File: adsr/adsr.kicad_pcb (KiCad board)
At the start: 2 copper layers, 44 parts, among them J1 B_GATE, J2 A_GATE, J3 B_IN, J4 A_IN, J5 B_OUT, J6 A_OUT, J7 EURORACK_CONN_16, J8 Conn_01x04_Male, Q1 2N3904, Q2 2N3904, Q3 2N3904, Q4 2N3904, U1 LM13700, U2 TL074, U3 DG403, U4 DG403, U5 DG403, U6 DG403

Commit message: rework ASDR
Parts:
- removed C3: 22u, Resistor_THT:R_Axial_DIN0204_L3.6mm_D1.6mm_P2.54mm_Vertical
- removed C4: 100n, Capacitor_THT:C_Rect_L10.0mm_W2.5mm_P7.50mm_MKS4
- removed D2: D, Diode_THT:D_A-405_P7.62mm_Horizontal
- removed Q3, Q4: 2N3904, Package_TO_SOT_THT:TO-92_Inline
- removed R10, R11, R9: 100K, Resistor_THT:R_Axial_DIN0204_L3.6mm_D1.6mm_P2.54mm_Vertical
- removed R12, R8: 1K, Resistor_THT:R_Axial_DIN0204_L3.6mm_D1.6mm_P2.54mm_Vertical
- removed R7: 12K, Resistor_THT:R_Axial_DIN0204_L3.6mm_D1.6mm_P2.54mm_Vertical
- removed RV5: R_SUSTAIN, Connector_PinHeader_2.54mm:PinHeader_1x03_P2.54mm_Vertical
- removed RV6: R_DECAY, Connector_PinHeader_2.54mm:PinHeader_1x03_P2.54mm_Vertical
- removed RV7: R_ATTACK, Connector_PinHeader_2.54mm:PinHeader_1x03_P2.54mm_Vertical
- removed RV8: R_RELEASE, Connector_PinHeader_2.54mm:PinHeader_1x03_P2.54mm_Vertical
- removed U5, U6: DG403, Package_SO:SOIC-16_3.9x9.9mm_P1.27mm
- added C10: 0.1u, Capacitor_SMD:C_1206_3216Metric_Pad1.42x1.75mm_HandSolder, F.Cu at (95.0, 142.2)
- added C7: 0.1u, Capacitor_SMD:C_1206_3216Metric_Pad1.42x1.75mm_HandSolder, F.Cu at (104.8, 158.1)
- added C8: 0.1u, Capacitor_SMD:C_1206_3216Metric_Pad1.42x1.75mm_HandSolder, F.Cu at (104.8, 161.3)
- added C9: 0.1u, Capacitor_SMD:C_1206_3216Metric_Pad1.42x1.75mm_HandSolder, F.Cu at (95.0, 145.4)
- added D3: D, Diode_THT:D_A-405_P2.54mm_Vertical_AnodeUp, F.Cu at (3.56, 71.2)
- added D4: D, Diode_THT:D_A-405_P2.54mm_Vertical_AnodeUp, F.Cu at (3.30, 85.2)
- added J10: Conn_01x08_Male, Connector_PinSocket_2.54mm:PinSocket_1x08_P2.54mm_Vertical, F.Cu at (-18.4, 112.4)
- added J11: Conn_01x08_Female, Connector_PinSocket_2.54mm:PinSocket_1x08_P2.54mm_Vertical, F.Cu at (71.8, 157.2)
- added J12: Conn_01x08_Male, Connector_PinSocket_2.54mm:PinSocket_1x08_P2.54mm_Vertical, F.Cu at (-15.9, 112.4)
- added J9: Conn_01x08_Female, Connector_PinSocket_2.54mm:PinSocket_1x08_P2.54mm_Vertical, F.Cu at (69.2, 157.2)
- added Q5: DMMT5401, Package_TO_SOT_SMD:SOT-23-6_Handsoldering, F.Cu at (109.9, 176.5)
- added R13: 1M, Resistor_SMD:R_1206_3216Metric_Pad1.42x1.75mm_HandSolder, F.Cu at (3.56, 76.3)
- added R14: 1M, Resistor_SMD:R_1206_3216Metric_Pad1.42x1.75mm_HandSolder, F.Cu at (3.30, 90.3)
- added R15: 10K, Resistor_SMD:R_1206_3216Metric_Pad1.42x1.75mm_HandSolder, F.Cu at (79.0, 160.0)
- added R16: 10K, Resistor_SMD:R_1206_3216Metric_Pad1.42x1.75mm_HandSolder, F.Cu at (79.0, 155.6)
- added R19: 6.8k, Resistor_SMD:R_1206_3216Metric_Pad1.42x1.75mm_HandSolder, F.Cu at (111.8, 170.2)
- C1: value 22u -> 4.7u; footprint Resistor_THT:R_Axial_DIN0204_L3.6mm_D1.6mm_P2.54mm_Vertical -> Capacitor_SMD:C_1206_3216Metric_Pad1.42x1.75mm_HandSolder
- C2: footprint Capacitor_THT:C_Rect_L10.0mm_W2.5mm_P7.50mm_MKS4 -> Capacitor_SMD:C_1206_3216Metric_Pad1.42x1.75mm_HandSolder
- D1: footprint Diode_THT:D_A-405_P7.62mm_Horizontal -> Diode_THT:D_A-405_P2.54mm_Vertical_AnodeUp
- J1, J2, J3, J4, J5, J6: footprint synth:3.5MM_Jack_Breakout_Vertical -> synth:Jack_3.5mm_QingPu_WQP-PJ398SM_Vertical_CircularHoles
- R1: value 12K -> 6.8k; footprint Resistor_THT:R_Axial_DIN0204_L3.6mm_D1.6mm_P2.54mm_Vertical -> Resistor_SMD:R_1206_3216Metric_Pad1.42x1.75mm_HandSolder
- R2, R3, R4, R5, R6: footprint Resistor_THT:R_Axial_DIN0204_L3.6mm_D1.6mm_P2.54mm_Vertical -> Resistor_SMD:R_1206_3216Metric_Pad1.42x1.75mm_HandSolder
- RV1: value R_SUSTAIN -> R_ATTACK; footprint Connector_PinHeader_2.54mm:PinHeader_1x03_P2.54mm_Vertical -> synth:Potentiometer_Alpha_RD902F-40-00D_Dual_Vertical
- RV2, RV4: footprint Connector_PinHeader_2.54mm:PinHeader_1x03_P2.54mm_Vertical -> synth:Potentiometer_Alpha_RD902F-40-00D_Dual_Vertical
- RV3: value R_ATTACK -> R_SUSTAIN; footprint Connector_PinHeader_2.54mm:PinHeader_1x03_P2.54mm_Vertical -> synth:Potentiometer_Alpha_RD902F-40-00D_Dual_Vertical
- moved RV3 201.7 mm to (-5.12, 100.3), turned to 270 degrees
- moved RV1 200.9 mm to (-5.12, 59.7), turned to 270 degrees
- moved RV2 200.2 mm to (-5.12, 80.0), turned to 270 degrees
- moved RV4 196.6 mm to (-5.12, 120.7), turned to 270 degrees
- moved R3 178.3 mm to (79.0, 169.5)
- moved Q2 158.5 mm to (125.7, 156.2), turned to 270 degrees
- moved R2 153.8 mm to (78.7, 165.7), turned to 180 degrees
- moved J8 146.6 mm to (1.91, 54.0)
- moved R1 143.1 mm to (107.3, 170.0), turned to 90 degrees
- moved C1 138.6 mm to (107.5, 151.8)
- moved C2 132.6 mm to (119.8, 156.2)
- moved R6 128.8 mm to (125.3, 163.6), turned to 270 degrees
- moved J7 128.0 mm to (99.1, 128.3)
- moved R4 128.0 mm to (133.3, 163.4), turned to 90 degrees
- moved Q1 125.1 mm to (132.7, 156.2), turned to 270 degrees
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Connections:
- J8 pad 1: B_OUT_DEFAULT -> A_IN_DEFAULT
- J8 pad 4: A_IN_DEFAULT -> B_OUT_DEFAULT
- R1 pad 1: Net-(R1-Pad1) -> Net-(Q5-Pad4)
- R2 pad 1: A_IN -> /envelope/REF
- RV1 pad 1: A_IN -> /sheet5F5D80AF/ATTACK
- RV1 pad 2: Net-(RV1-Pad2) -> GND
- RV2 pad 1: +12V -> /sheet5F5D80AF/DECAY
- RV2 pad 2: +12V -> GND
- RV2 pad 3: Net-(RV2-Pad3) -> GND
- RV3 pad 1: +12V -> GND
- RV3 pad 2: +12V -> /sheet5F5D80AF/SUS_RAW
- RV3 pad 3: Net-(RV3-Pad3) -> /sheet5F5D80AF/REF_RAW
- RV4 pad 1: +12V -> /sheet5F5D80AF/RELEASE
- RV4 pad 2: +12V -> GND
- RV4 pad 3: Net-(RV4-Pad3) -> GND
- U2 pad 10: Net-(R8-Pad2) -> /envelope/REF_RAW
- U2 pad 12: Net-(C3-Pad1) -> /envelope/SUS_RAW
- U2 pad 13: B_OUT -> /envelope/SUS
- U2 pad 14: B_OUT -> /envelope/SUS
- U2 pad 6: A_OUT -> Net-(R15-Pad2)
- U2 pad 8: Net-(U1-Pad7) -> /envelope/REF
- U2 pad 9: Net-(C3-Pad1) -> /envelope/REF
- U3 pad 6: Net-(RV1-Pad2) -> /envelope/SUS
- U3 pad 8: A_IN -> /envelope/REF
- U4 pad 1: Net-(RV4-Pad3) -> /envelope/RELEASE
- U4 pad 16: Net-(R1-Pad1) -> Net-(R19-Pad2)
- U4 pad 4: Net-(R1-Pad1) -> Net-(R19-Pad2)
- U4 pad 6: Net-(RV2-Pad3) -> /envelope/DECAY
- U4 pad 8: Net-(RV3-Pad3) -> /envelope/ATTACK
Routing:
- net A_GATE: track 0.00 -> 81.4 mm
- net B_GATE: track 0.00 -> 81.2 mm
- net /envelope/ATTACK: track 0.00 -> 77.1 mm, vias 0 -> 1
- net B_OUT: track 0.00 -> 73.6 mm
- net A_OUT: track 0.00 -> 73.6 mm
- net /sheet5F5D80AF/ATTACK: track 0.00 -> 62.9 mm
- net B_IN: track 0.00 -> 61.7 mm
- net /envelope/REF_RAW: track 0.00 -> 55.5 mm
- net /envelope/DECAY: track 0.00 -> 49.7 mm
- net A_IN: track 0.00 -> 49.3 mm
- net /sheet5F5D80AF/DECAY: track 0.00 -> 45.1 mm
- net /sheet5F5D80AF/REF_RAW: track 0.00 -> 44.7 mm
- net A_IN_DEFAULT: track 0.00 -> 39.5 mm
- net B_IN_DEFAULT: track 0.00 -> 34.2 mm
- net /envelope/SUS_RAW: track 0.00 -> 32.8 mm
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- added copper zone on B.Cu, net GND
- added copper zone on F.Cu, net GND
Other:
- board outline added: 29.2 x 112.4 mm
- board text added: "TODO: maybe centering would be better for both trace length and structural?"

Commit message: more layout
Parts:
- added J8: Conn_01x04_Male, Connector_PinHeader_2.54mm:PinHeader_2x02_P2.54mm_Vertical, F.Cu at (104.1, 51.4)
- J7: moved to B.Cu
- moved U4 137.7 mm to (84.6, 35.8)
- moved C8 137.7 mm to (96.5, 23.8), turned to 270 degrees
- moved C7 134.8 mm to (92.5, 23.8), turned to 90 degrees
- moved U2 123.5 mm to (90.4, 32.5), turned to 0 degrees
- moved U3 123.3 mm to (84.6, 49.5)
- moved R3 118.5 mm to (126.2, 60.9), turned to 90 degrees
- moved R15 118.3 mm to (123.2, 50.3), turned to 270 degrees
- moved R4 113.5 mm to (119.6, 50.8), turned to 270 degrees
- moved R19 112.4 mm to (89.4, 60.0)
- moved Q5 111.5 mm to (94.0, 66.2), turned to 270 degrees
- moved R16 111.4 mm to (116.6, 50.8), turned to 90 degrees
- moved R6 110.9 mm to (85.9, 60.0)
- moved R2 107.8 mm to (104.1, 60.9), turned to 90 degrees
- moved R5 106.8 mm to (85.9, 66.0)
- moved R1 105.4 mm to (89.4, 66.1), turned to 270 degrees
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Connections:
- U2 pad 1: Net-(U1-Pad10) -> /envelope/REF
- U2 pad 10: /envelope/REF_RAW -> Net-(R2-Pad2)
- U2 pad 12: /envelope/SUS_RAW -> Net-(C1-Pad1)
- U2 pad 13: /envelope/SUS -> Net-(R15-Pad2)
- U2 pad 14: /envelope/SUS -> A_OUT
- U2 pad 2: Net-(C1-Pad1) -> /envelope/REF
- U2 pad 3: Net-(R2-Pad2) -> /envelope/REF_RAW
- U2 pad 5: Net-(C1-Pad1) -> /envelope/SUS_RAW
- U2 pad 6: Net-(R15-Pad2) -> /envelope/SUS
- U2 pad 7: A_OUT -> /envelope/SUS
- U2 pad 8: /envelope/REF -> Net-(U1-Pad10)
- U2 pad 9: /envelope/REF -> Net-(C1-Pad1)
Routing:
- net B_OUT: track 73.6 -> 29.3 mm
- net B_GATE: track 81.2 -> 37.0 mm
- net /sheet5F5D80AF/ATTACK: track 62.9 -> 18.9 mm
- net A_OUT: track 73.6 -> 30.0 mm
- net /envelope/ATTACK: track 77.1 -> 33.5 mm
- net A_GATE: track 81.4 -> 38.2 mm
- net /envelope/DECAY: track 49.7 -> 15.3 mm
- net /sheet5F5D80AF/DECAY: track 45.1 -> 13.9 mm
- net /sheet5F5D80AF/RELEASE: track 14.4 -> 42.5 mm
- net /envelope/RELEASE: track 19.1 -> 40.1 mm
- net B_IN: track 61.7 -> 42.4 mm
- net /sheet5F5D80AF/REF_RAW: track 44.7 -> 54.5 mm
- net /envelope/REF_RAW: track 55.5 -> 45.8 mm
- net Net-(C1-Pad1): track 0.00 -> 8.55 mm
- net /envelope/SUS_RAW: track 32.8 -> 24.7 mm
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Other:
- board size 29.2 x 112.4 mm -> 94.6 x 114.9 mm

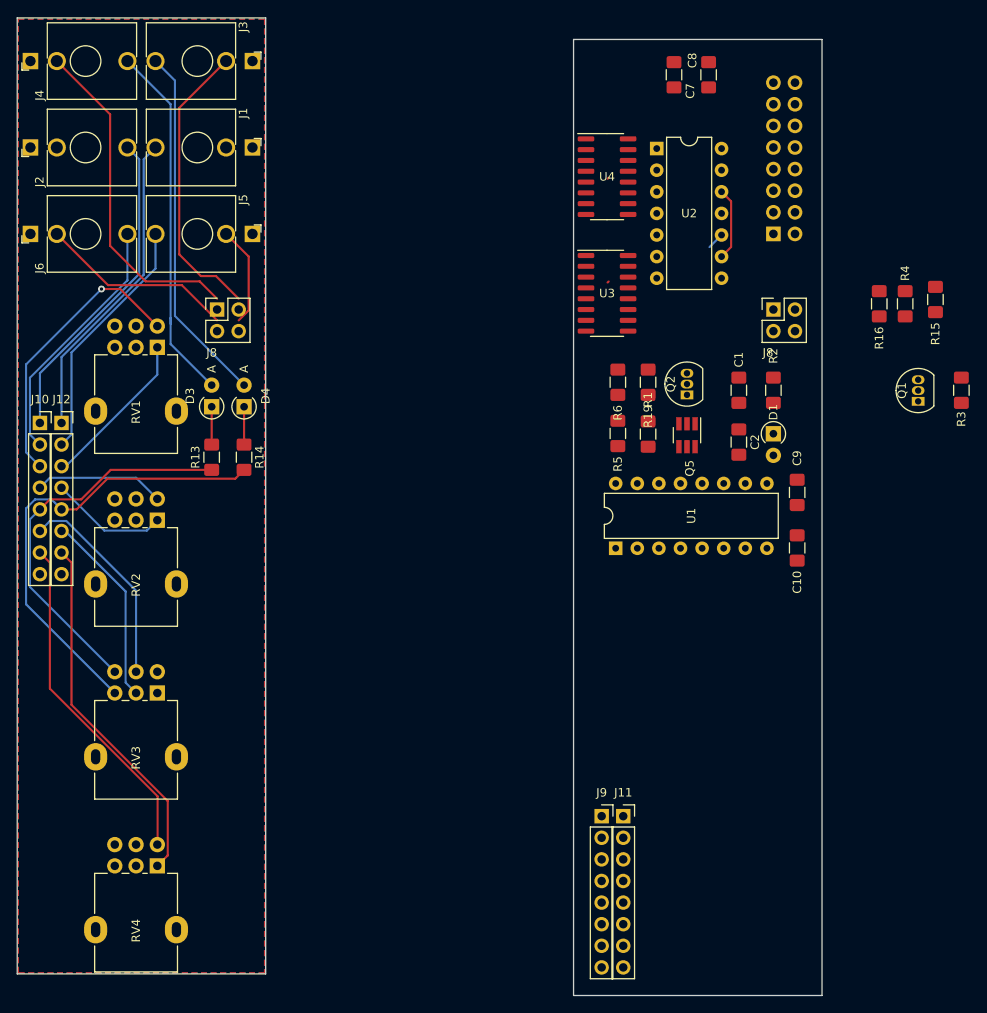
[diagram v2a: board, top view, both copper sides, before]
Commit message: reduce to one input
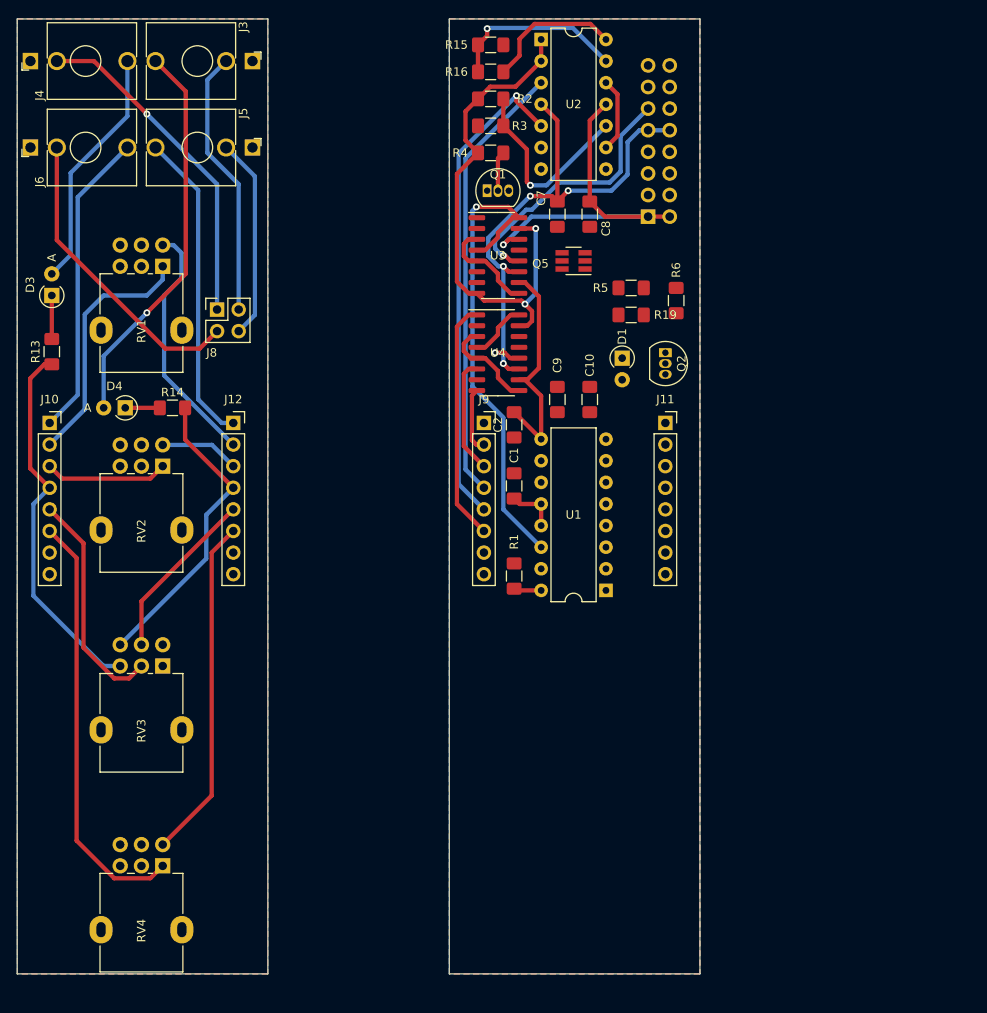
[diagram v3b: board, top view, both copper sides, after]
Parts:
- removed J1: B_GATE, synth:Jack_3.5mm_QingPu_WQP-PJ398SM_Vertical_CircularHoles
- removed J2: A_GATE, synth:Jack_3.5mm_QingPu_WQP-PJ398SM_Vertical_CircularHoles
- removed the J8 at (104.1, 51.4)
- moved R3 63.5 mm to (70.9, 29.8), turned to 180 degrees
- moved R15 60.3 mm to (70.9, 20.3), turned to 180 degrees
- moved Q1 56.4 mm to (70.5, 37.5), turned to 0 degrees
- moved R16 53.2 mm to (70.9, 23.5), turned to 0 degrees
- moved R4 51.9 mm to (70.9, 33.0), turned to 0 degrees
- moved J9 48.3 mm to (70.1, 64.8)
- moved R2 47.7 mm to (70.9, 26.7), turned to 0 degrees
- moved J11 46.5 mm to (91.4, 64.8)
- moved C9 30.2 mm to (78.7, 62.0)
- moved C10 30.0 mm to (82.5, 62.0), turned to 270 degrees
- moved C1 28.7 mm to (73.7, 72.2)
- moved C2 26.5 mm to (73.7, 65.0), turned to 270 degrees
- moved Q5 24.5 mm to (80.6, 45.7), turned to 180 degrees
- moved U4 24.4 mm to (71.8, 56.5)
- moved R1 22.9 mm to (73.7, 82.8)
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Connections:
- J10 pad 1: A_GATE -> A_OUT
- J10 pad 2: A_OUT -> /envelope/ATTACK
- J10 pad 3: /envelope/ATTACK -> /envelope/DECAY
- J10 pad 4: /envelope/DECAY -> /envelope/REF_RAW
- J10 pad 5: /envelope/REF_RAW -> /envelope/SUS_RAW
- J10 pad 6: /envelope/SUS_RAW -> /envelope/RELEASE
- J10 pad 7: /envelope/RELEASE -> GND
- J11 pad 1: B_GATE -> B_OUT
- J11 pad 2: B_OUT -> /sheet5F5D80AF/ATTACK
- J11 pad 3: /sheet5F5D80AF/ATTACK -> /sheet5F5D80AF/DECAY
- J11 pad 4: /sheet5F5D80AF/DECAY -> /sheet5F5D80AF/REF_RAW
- J11 pad 5: /sheet5F5D80AF/REF_RAW -> /sheet5F5D80AF/SUS_RAW
- J11 pad 6: /sheet5F5D80AF/SUS_RAW -> /sheet5F5D80AF/RELEASE
- J11 pad 7: /sheet5F5D80AF/RELEASE -> GND
- J12 pad 1: B_GATE -> B_OUT
- J12 pad 2: B_OUT -> /sheet5F5D80AF/ATTACK
- J12 pad 3: /sheet5F5D80AF/ATTACK -> /sheet5F5D80AF/DECAY
- J12 pad 4: /sheet5F5D80AF/DECAY -> /sheet5F5D80AF/REF_RAW
- J12 pad 5: /sheet5F5D80AF/REF_RAW -> /sheet5F5D80AF/SUS_RAW
- J12 pad 6: /sheet5F5D80AF/SUS_RAW -> /sheet5F5D80AF/RELEASE
- J12 pad 7: /sheet5F5D80AF/RELEASE -> GND
- J9 pad 1: A_GATE -> A_OUT
- J9 pad 2: A_OUT -> /envelope/ATTACK
- J9 pad 3: /envelope/ATTACK -> /envelope/DECAY
- J9 pad 4: /envelope/DECAY -> /envelope/REF_RAW
- J9 pad 5: /envelope/REF_RAW -> /envelope/SUS_RAW
- J9 pad 6: /envelope/SUS_RAW -> /envelope/RELEASE
- J9 pad 7: /envelope/RELEASE -> GND
- R4 pad 1: A_GATE -> /envelope/REF
- RV1 pad 1: /sheet5F5D80AF/ATTACK -> /envelope/ATTACK
- RV1 pad 4: /envelope/ATTACK -> /sheet5F5D80AF/ATTACK
- RV2 pad 1: /sheet5F5D80AF/DECAY -> /envelope/DECAY
- RV2 pad 4: /envelope/DECAY -> /sheet5F5D80AF/DECAY
- RV3 pad 2: /sheet5F5D80AF/SUS_RAW -> /envelope/SUS_RAW
- RV3 pad 3: /sheet5F5D80AF/REF_RAW -> /envelope/REF_RAW
- RV3 pad 5: /envelope/SUS_RAW -> /sheet5F5D80AF/SUS_RAW
- RV3 pad 6: /envelope/REF_RAW -> /sheet5F5D80AF/REF_RAW
- RV4 pad 1: /sheet5F5D80AF/RELEASE -> /envelope/RELEASE
- RV4 pad 4: /envelope/RELEASE -> /sheet5F5D80AF/RELEASE
- U3 pad 15: A_GATE -> /envelope/REF
- U4 pad 15: A_GATE -> /envelope/REF
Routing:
- net +12V: track 0.00 -> 61.8 mm, vias 0 -> 4
- net /envelope/REF: track 0.00 -> 60.1 mm, vias 0 -> 2
- net /envelope/SUS_RAW: track 24.7 -> 84.3 mm, vias 0 -> 1
- net Net-(U1-Pad14): track 0.00 -> 55.9 mm, vias 0 -> 1
- net /envelope/REF_RAW: track 45.8 -> 96.3 mm
- net -12V: track 0.00 -> 42.8 mm, vias 0 -> 1
- net /envelope/RELEASE: track 40.1 -> 78.5 mm
- net A_GATE: track 38.2 -> 0.00 mm
- net B_GATE: track 37.0 -> 0.00 mm
- net +5V: track 0.00 -> 34.3 mm, vias 0 -> 2
- net /envelope/STATE: track 0.00 -> 27.3 mm
- net A_OUT: track 30.0 -> 52.5 mm
- net Net-(R2-Pad2): track 2.00 -> 23.3 mm, vias 0 -> 1
- net Net-(R15-Pad2): track 0.00 -> 21.1 mm, vias 0 -> 1
- net /sheet5F5D80AF/REF_RAW: track 54.5 -> 35.7 mm
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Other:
- board size 94.6 x 114.9 mm -> 80.3 x 112.3 mm
- net class Default: clearance 0.2 -> 0.3048; trace_width 0.25 -> 0.508; via_dia 0.8 -> 0.8128; via_drill 0.4 -> 0.4064
- rule trace_clearance: 0.2 -> 0.3048
- board text removed: "TODO: maybe centering would be better for both trace length and structural?"

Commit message: layout
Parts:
- moved U2 33.5 mm to (76.8, 53.2)
- moved R2 31.4 mm to (71.3, 58.0), turned to 180 degrees
- moved R3 31.4 mm to (71.3, 61.2), turned to 0 degrees
- moved R15 28.5 mm to (71.4, 48.8)
- moved R16 28.3 mm to (71.4, 51.8)
- moved U4 27.9 mm to (86.9, 33.0), turned to 90 degrees
- moved R4 21.8 mm to (71.3, 54.9), turned to 180 degrees
- moved Q1 19.0 mm to (88.9, 42.2), turned to 270 degrees
- moved J7 17.1 mm to (89.4, 23.4), turned to 90 degrees
- moved C10 13.7 mm to (83.8, 75.7), turned to 180 degrees
- moved C9 13.7 mm to (77.9, 75.7), turned to 180 degrees
- moved U3 12.5 mm to (75.2, 33.0), turned to 90 degrees
- moved C1 12.2 mm to (73.7, 84.4)
- moved C2 12.2 mm to (73.7, 77.2)
- moved R1 12.2 mm to (73.7, 95.0)
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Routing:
- net +12V: track 61.8 -> 205.6 mm, vias 4 -> 7
- net -12V: track 42.8 -> 156.8 mm, vias 1 -> 3
- net /envelope/STATE: track 27.3 -> 85.6 mm, vias 0 -> 3
- net Net-(Q5-Pad4): track 0.00 -> 48.9 mm, vias 0 -> 2
- net /envelope/ATTACK: track 37.1 -> 82.4 mm
- net /envelope/SUS_RAW: track 84.3 -> 41.2 mm, vias 1 -> 0
- net /envelope/DECAY: track 28.1 -> 68.4 mm
- net /envelope/REF_RAW: track 96.3 -> 61.2 mm
- net /envelope/SUS: track 0.00 -> 34.0 mm, vias 0 -> 1
- net Net-(R2-Pad2): track 23.3 -> 53.4 mm
- net Net-(C1-Pad1): track 14.7 -> 43.3 mm, vias 0 -> 1
- net Net-(Q1-Pad2): track 4.71 -> 33.1 mm, vias 0 -> 2
- net /envelope/RELEASE: track 78.5 -> 103.3 mm, vias 0 -> 1
- net A_OUT: track 52.5 -> 74.0 mm, vias 0 -> 3
- net Net-(U1-Pad14): track 55.9 -> 74.1 mm
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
